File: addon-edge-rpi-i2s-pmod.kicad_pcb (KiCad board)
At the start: 2 copper layers, 100 x 72 mm, 38 parts, among them J1 PMOD1, J10 Conn_01x02, J11 Conn_01x01, J2 PMOD2, J3 PMOD3, J4 Conn_01x06, J5 Conn_01x06, J6 Conn_02x04_Top_Bottom, J7 Conn_01x03, J8 Conn_01x04, J9 Conn_01x05

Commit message: update 10/02/22 initial autorouting
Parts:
- moved J11 1.91 mm to (189.2, 134.6)
- renumbered REF** to OH2
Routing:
- net /A2_CE1: track 0.00 -> 129.0 mm, vias 0 -> 1
- net /B13_SCLK_DABD: track 0.00 -> 114.2 mm
- net /A27_DIN_I2S: track 0.00 -> 111.4 mm
- net /B16_UART_TX_MIDI: track 0.00 -> 111.0 mm, vias 0 -> 1
- net /B14_CE0_CLKBD: track 0.00 -> 110.4 mm, vias 0 -> 2
- net /3V3pi: track 0.00 -> 104.4 mm, vias 0 -> 1
- net /A1_MOSI: track 0.00 -> 104.2 mm
- net /A28_MISO_WSBD: track 0.00 -> 100.7 mm
- net /DAC_BCLK_I2S: track 0.00 -> 100.7 mm
- net /B1_UART_RX: track 0.00 -> 99.9 mm
- net /B1_CE2_UART_RX: track 0.00 -> 99.2 mm, vias 0 -> 2
- net /B1_SPI1_CE2: track 0.00 -> 96.1 mm, vias 0 -> 1
- net +5V: track 0.00 -> 95.4 mm
- net /B26_WSEL_LRCLK_I2S: track 0.00 -> 91.6 mm, vias 0 -> 1
- net /DAC_DIN_I2S: track 0.00 -> 90.2 mm, vias 0 -> 2
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
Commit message: rev 0.40
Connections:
- net /B16_PMOD renamed /B16_PMOD2_D3
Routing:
- net GND: track 15.4 -> 40.1 mm, vias 2 -> 3
- net /A1_MOSI: track 104.2 -> 91.6 mm
- net /B1_CE2_UART_RX: track 99.2 -> 92.8 mm
- net /B13_SCLK_DABD: track 114.2 -> 119.3 mm
- net /3V3pi: track 104.4 -> 109.1 mm
- net /PIMIDI_B3_CLK: track 68.9 -> 73.5 mm
- net /B26_WSEL_LRCLK_I2S: track 91.6 -> 95.4 mm, vias 1 -> 3
- net /A27_DIN_I2S: track 111.4 -> 115.0 mm
- net /DAC_BCLK_I2S: track 100.7 -> 104.1 mm
- net /5Vpi: track 57.3 -> 60.6 mm, vias 0 -> 1
- net /PIMIDI_BUT5: track 75.2 -> 78.5 mm
- net /A1_SPI1_MOSI: track 56.7 -> 59.9 mm
- net /PIMIDI_B4_DAT: track 64.4 -> 66.7 mm
- net /A2_CE1: track 129.0 -> 131.3 mm
- net +3V3: track 55.5 -> 57.4 mm
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- added copper zone on F.Cu, net GND
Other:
- board text added: "MIDI I2S SBC Pmod Edge Interface v${VERSION}"
- board text removed: "BYPASS JUMPERS: LEAVE DISCONNECTED. ONLY CONNECT WITHOUT AN FPGA ATTACHED"
- board text removed: "MIDI I2S SBC Pmod Edge Interface v0.1"

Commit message: rev. 0.41
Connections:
- net /3V3pi renamed 3V3pi
- net /5Vpi renamed 5Vpi
- net /VIN renamed VIN
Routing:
- net GND: track 40.1 -> 38.8 mm
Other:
- board text added: "C0"
- board text added: "C1"
- board text added: "C2"
- board text added: "CK"
- board text added: "FPGA/RPI"
- board text added: "MI"
- board text added: "MO"
- board text added: "SPI0"
- board text removed: "MULTICORE"
- board text removed: "RPI"

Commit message: modified jumper spacing for allowing switches
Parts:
- moved JP45 1.00 mm to (119.9, 99.3)
- moved JP44 0.75 mm to (119.9, 108.4)
- moved JP43 0.50 mm to (119.9, 117.6)
- moved JP42 0.25 mm to (119.9, 126.7)
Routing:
- net /A2_SPI1_CE1: track 63.1 -> 64.1 mm
- net /A2_CE1: track 131.3 -> 132.3 mm
- net /B14_CE0_CLKBD: track 109.9 -> 110.9 mm
- net /B13_SCLK_DABD: track 119.3 -> 119.8 mm
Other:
- board text added: "DAC SOURCE"
- board text added: "RPI"
- board text removed: "DAC SOURCE SELECTION"

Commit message: v0.50 major changes
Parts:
- removed the J6 at (143.5, 116.8)
- removed JP31, JP32: Conn_01x03, Connector_PinHeader_2.54mm:PinHeader_1x03_P2.54mm_Vertical
- added J12: Conn_01x02, Connector_PinSocket_2.54mm:PinSocket_2x01_P2.54mm_Horizontal, F.Cu at (196.2, 102.9)
- added J4: PMOD4, gomaDOSzero:PMOD_Female_Horizontal_2, F.Cu at (196.2, 97.8)
- added JPS1: SolderJumper_3_Open, Jumper:SolderJumper-3_P1.3mm_Open_RoundedPad1.0x1.5mm_NumberLabels, B.Cu at (146.1, 108.0)
- added JPS2: SolderJumper_3_Open, Jumper:SolderJumper-3_P1.3mm_Open_RoundedPad1.0x1.5mm_NumberLabels, B.Cu at (146.1, 102.2)
- J8: footprint gomaDOSzero:OLED_091_DISPLAY -> gomaDOSzero:I2C_DISPLAY_MULTI2
- JP12: value Conn_01x03 -> Conn_01x02; footprint Connector_PinHeader_2.54mm:PinHeader_1x03_P2.54mm_Horizontal -> Connector_PinHeader_2.54mm:PinHeader_1x02_P2.54mm_Horizontal
- moved LO4 85.4 mm to (127.6, 132.7)
- moved BUT1 72.3 mm to (176.4, 48.9), turned to -90 degrees
- moved R1 59.2 mm to (174.2, 60.3), turned to 180 degrees
- moved BUT2 53.6 mm to (176.4, 67.3), turned to -90 degrees
- moved LO3 43.8 mm to (191.8, 61.0)
- moved R2 42.1 mm to (174.2, 78.7), turned to 180 degrees
- moved J6 37.0 mm to (196.2, 78.7), turned to -90 degrees
- moved JP5 36.2 mm to (187.3, 102.9)
- moved JP11 31.5 mm to (145.4, 55.9)
- moved J5 31.5 mm to (164.5, 76.2)
- moved JP12 30.7 mm to (160.0, 55.9)
- moved J7 30.7 mm to (206.4, 132.7)
- moved H1 27.7 mm to (205.1, 48.9)
- moved LO2 26.1 mm to (174.0, 89.5)
- moved J9 21.9 mm to (206.4, 65.4)
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- renumbered J11 to J13, J4 to J5, J5 to J6, REF** to LO1, OH2 to LO2, OH1 to LO3, ESD1 to LO4
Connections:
- net Net-(J3-Pad12) renamed /VH_PMOD
- EDGE1 pad A12: /A12_PMOD1_D2 -> /A12_PMOD1_D6
- EDGE1 pad A20: /A20_PMOD2_D4 -> /A20_PMOD2_D5
- EDGE1 pad A21: /A21_PMOD2_D0 -> /A21_PMOD2_D1
- EDGE1 pad A22: /A22_PMOD2_D1 -> /A22_PMOD2_D6
- EDGE1 pad A23: /A23_PMOD2_D5 -> /A23_PMOD2_D2
- EDGE1 pad A24: /A24_PMOD2_D2 -> /A24_PMOD2_D7
- EDGE1 pad A25: /A25_PMOD2_D6 -> /A25_PMOD2_D3
- EDGE1 pad B1: /B1_CE2_UART_RX -> /B1_UART_RX
- EDGE1 pad B10: unconnected-(EDGE1-PadB10) -> /B10_SRAMDQ13
- EDGE1 pad B11: unconnected-(EDGE1-PadB11) -> /B11_SRAMDQ11
- EDGE1 pad B12: unconnected-(EDGE1-PadB12) -> /B12_SRAMDQ12
- EDGE1 pad B15: unconnected-(EDGE1-PadB15) -> /B15_SCL_PM1_D2
- EDGE1 pad B16: /B16_PMOD_UARTX_MIDI -> /B16_UART_TX_MIDI
- EDGE1 pad B17: /B17_PMOD1_D6 -> /B17_PMOD1_D7
- EDGE1 pad B18: /B18_PMOD1_D3 -> /B18_PMOD2_D4
- EDGE1 pad B19: /B19_PMOD1_D7 -> /B19_PMOD2_D0
- EDGE1 pad B21: unconnected-(EDGE1-PadB21) -> /B21_SDA_PM1_D3
- EDGE1 pad B27: /B27_PMOD2_D7 -> /B27_SPI1CE2
- EDGE1 pad B3: unconnected-(EDGE1-PadB3) -> /B3_SRAMDQ15
- EDGE1 pad B6: unconnected-(EDGE1-PadB6) -> /B6_SRAMDQ8
- EDGE1 pad B7: unconnected-(EDGE1-PadB7) -> /B7_SRAMDQ9
- EDGE1 pad B8: unconnected-(EDGE1-PadB8) -> /B8_SRAMDQ10
- EDGE1 pad B9: unconnected-(EDGE1-PadB9) -> /B9_SRAMDQ14
- J1 pad 10: /B19_PMOD1_D7 -> /B17_PMOD1_D7
- J1 pad 3: /A12_PMOD1_D2 -> /B15_SCL_PM1_D2
- J1 pad 4: /B18_PMOD1_D3 -> /B21_SDA_PM1_D3
- J1 pad 9: /B17_PMOD1_D6 -> /A12_PMOD1_D6
- J2 pad 1: /A21_PMOD2_D0 -> /B19_PMOD2_D0
- J2 pad 10: /B27_PMOD2_D7 -> /A24_PMOD2_D7
- J2 pad 2: /A22_PMOD2_D1 -> /A21_PMOD2_D1
- J2 pad 3: /A24_PMOD2_D2 -> /A23_PMOD2_D2
- J2 pad 4: /B16_PMOD2_D3 -> /A25_PMOD2_D3
- J2 pad 7: /A20_PMOD2_D4 -> /B18_PMOD2_D4
- J2 pad 8: /A23_PMOD2_D5 -> /A20_PMOD2_D5
- J2 pad 9: /A25_PMOD2_D6 -> /A22_PMOD2_D6
- J3 pad 10: /B1_SPI1_CE2 -> /B27_SPI1CE2
- J8 pad 1: GND -> /DISPLAY_PS1
- J8 pad 2: 3V3pi -> /DISPLAY_PS2
- JP12 pad 1: VIN -> /JP11_Vout
- RPI1 pad 36: /B1_SPI1_CE2 -> /B27_SPI1CE2
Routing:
- net /A2_CE1: track 132.3 -> 0.00 mm, vias 1 -> 0
- net /B13_SCLK_DABD: track 119.8 -> 0.00 mm
- net /A27_DIN_I2S: track 115.0 -> 0.00 mm
- net /B14_CE0_CLKBD: track 110.9 -> 0.00 mm, vias 2 -> 0
- net /B16_UART_TX_MIDI: track 110.3 -> 0.00 mm, vias 1 -> 0
- net 3V3pi: track 109.1 -> 0.00 mm, vias 1 -> 0
- net /DAC_BCLK_I2S: track 104.1 -> 0.00 mm
- net /A28_MISO_WSBD: track 102.5 -> 0.00 mm
- net /B1_UART_RX: track 98.9 -> 0.00 mm
- net /B1_SPI1_CE2: track 95.7 -> 0.00 mm, vias 1 -> 0
- net /B26_WSEL_LRCLK_I2S: track 94.9 -> 0.00 mm, vias 3 -> 0
- net +5V: track 94.7 -> 0.00 mm
- net /B1_CE2_UART_RX: track 92.8 -> 0.00 mm, vias 2 -> 0
- net /A1_MOSI: track 91.6 -> 0.00 mm
- net /DAC_DIN_I2S: track 89.5 -> 0.00 mm, vias 2 -> 0
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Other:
- board size 100 x 72 mm -> 100 x 100 mm
- board text added: "(I2C)"
- board text added: "(SPI + UART)"
- board text added: "(SRAM NEPTUNO)"
- board text added: "10"
- board text added: "11"
- board text added: "12"
- board text added: "13"
- board text added: "14"
- board text added: "15"
- board text added: "8"
- board text added: "9"
- board text added: "CHECK 3V3 / GND SOLDER JUMPERS JPS1, JPS2"
- board text added: "DAC VIN SOURCE"
- board text added: "JP11"
- board text added: "MIDI2SBC Edge v${VERSION}"
- board text added: "OLED DISPLAY"
- board text added: "PS1"
- board text added: "PS2"
- board text added: "SCL"
- board text added: "SDA"
- board text removed: "CE2"
- board text removed: "DAC I2S VIN SELECTION"
- board text removed: "FPGA/RPI"
- board text removed: "J4.J5 / JP11"
- board text removed: "P2D3"
- board text removed: "POW.RPI"
- board text removed: "SPI0/SPI1"

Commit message: v0.51 manual routing finished
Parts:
- moved J13 7.73 mm to (189.9, 134.0)
- moved BUT1 0.91 mm to (176.4, 49.8)
- moved R1 0.91 mm to (174.2, 61.2)
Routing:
- net 3V3pi: track 0.00 -> 192.2 mm, vias 0 -> 1
- net +5V: track 0.00 -> 160.7 mm, vias 0 -> 2
- net /A2_SPI1_CE1: track 0.00 -> 145.6 mm
- net /A2_CE1: track 0.00 -> 133.1 mm, vias 0 -> 1
- net /B14_CE0_CLKBD: track 0.00 -> 131.8 mm, vias 0 -> 1
- net /B1_UART_RX: track 0.00 -> 128.8 mm, vias 0 -> 3
- net /A28_MISO_WSBD: track 0.00 -> 127.7 mm, vias 0 -> 1
- net /B13_SCLK_DABD: track 0.00 -> 124.3 mm, vias 0 -> 1
- net /B27_SPI1CE2: track 0.00 -> 118.0 mm
- net /B16_UART_TX_MIDI: track 0.00 -> 117.3 mm, vias 0 -> 4
- net /B26_WSEL_LRCLK_I2S: track 0.00 -> 116.1 mm, vias 0 -> 1
- net /A27_DIN_I2S: track 0.00 -> 115.7 mm, vias 0 -> 2
- net /B3_SRAMDQ15: track 0.00 -> 114.6 mm
- net 5Vpi: track 0.00 -> 105.9 mm, vias 0 -> 1
- net /B12_SRAMDQ12: track 0.00 -> 104.2 mm
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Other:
- board text added: "(SRAM NeptUNO)"
- board text added: "CHECK 3V3/GND SOLDER JUMPERS JPS1, JPS2"
- board text added: "ROM"
- board text added: "SYNTH"
- board text removed: "(SRAM NEPTUNO)"
- board text removed: "CHECK 3V3 / GND SOLDER JUMPERS JPS1, JPS2"

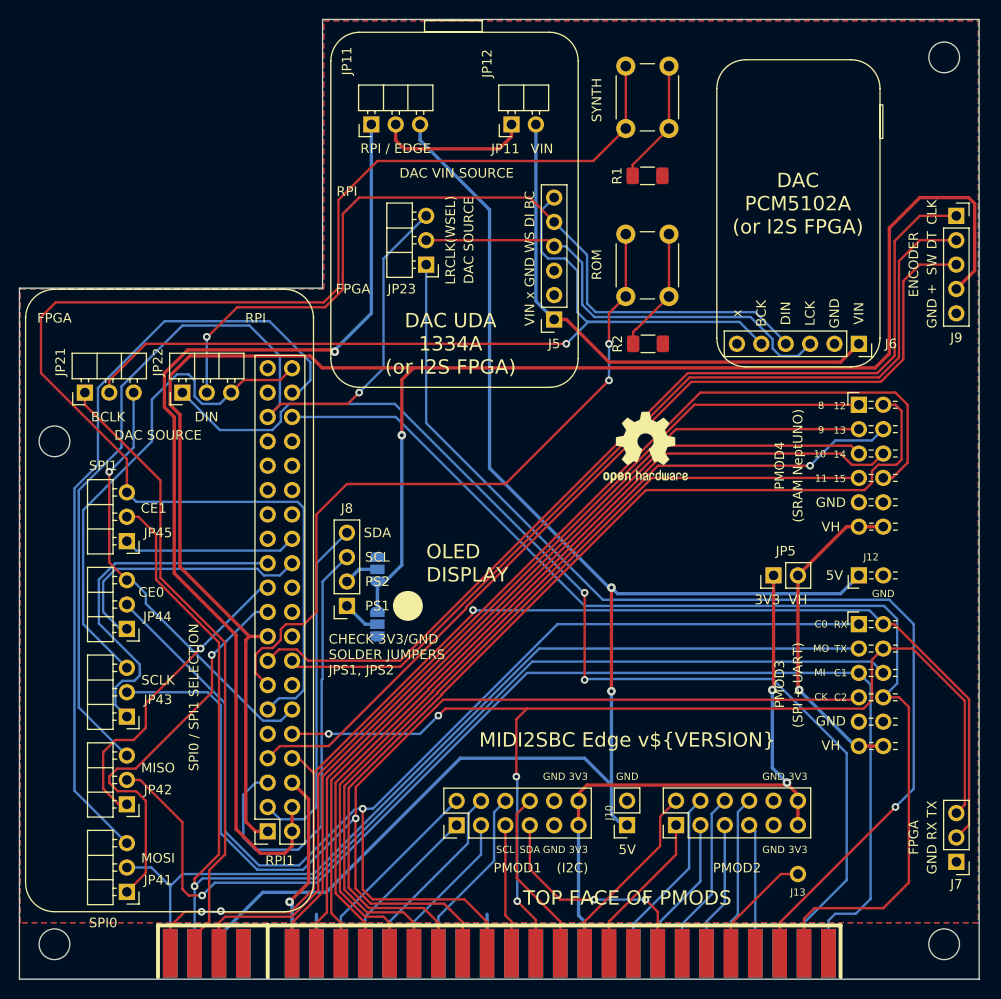
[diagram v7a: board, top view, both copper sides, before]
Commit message: v0.52 changed tracks pmod 1 & 2
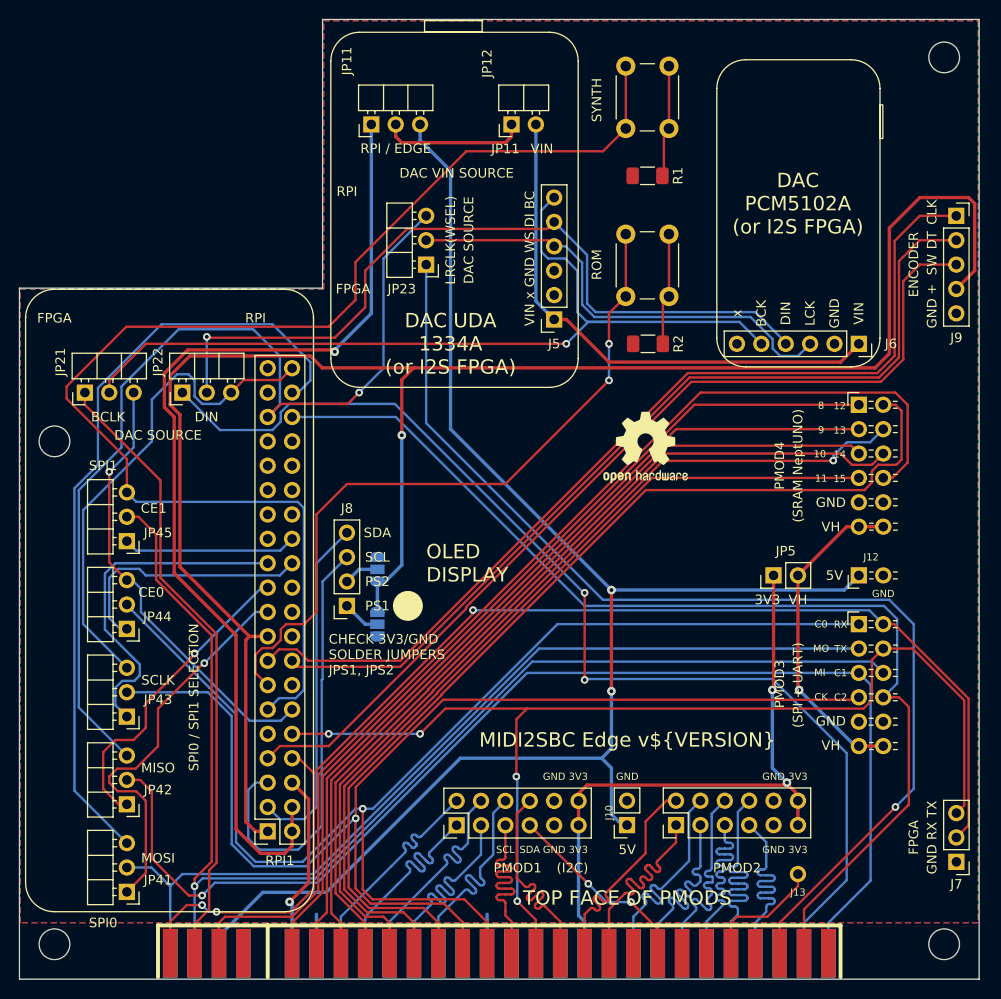
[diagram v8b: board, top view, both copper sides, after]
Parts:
- turned R1 to 0 degrees
- turned R2 to 0 degrees
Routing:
- net /A2_SPI1_CE1: track 145.6 -> 134.5 mm
- net /A24_PMOD2_D7: track 16.7 -> 27.6 mm
- net /A25_PMOD2_D3: track 13.6 -> 23.3 mm
- net /B15_SCL_PM1_D2: track 13.6 -> 23.2 mm
- net /A23_PMOD2_D2: track 14.1 -> 23.2 mm
- net /A21_PMOD2_D1: track 15.2 -> 23.3 mm
- net /A11_PMOD1_D1: track 16.2 -> 23.3 mm
- net /B19_PMOD2_D0: track 16.2 -> 23.3 mm
- net /A9_PMOD1_D0: track 17.3 -> 23.3 mm
- net /A22_PMOD2_D6: track 17.7 -> 23.2 mm
- net /B17_PMOD1_D7: track 18.3 -> 23.3 mm
- net /A12_PMOD1_D6: track 18.8 -> 23.4 mm
- net /A20_PMOD2_D5: track 18.8 -> 23.3 mm
- net /DAC_DIN_I2S: track 86.1 -> 81.7 mm
- net /B27_SPI1CE2: track 118.0 -> 113.8 mm
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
